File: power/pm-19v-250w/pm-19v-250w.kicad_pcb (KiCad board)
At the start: 4 copper layers, 58.4 x 22.9 mm, 58 parts, among them J1 Brick 1/8 (DOSA), J2 Aux, Q1 BSC070N10NS5, Q2 BSC070N10NS5, Q3 BSC070N10NS5, Q4 BSC070N10NS5, U1 LTC7810, U2 MCP65R46-1.21, U3 MCP65R46-1.21

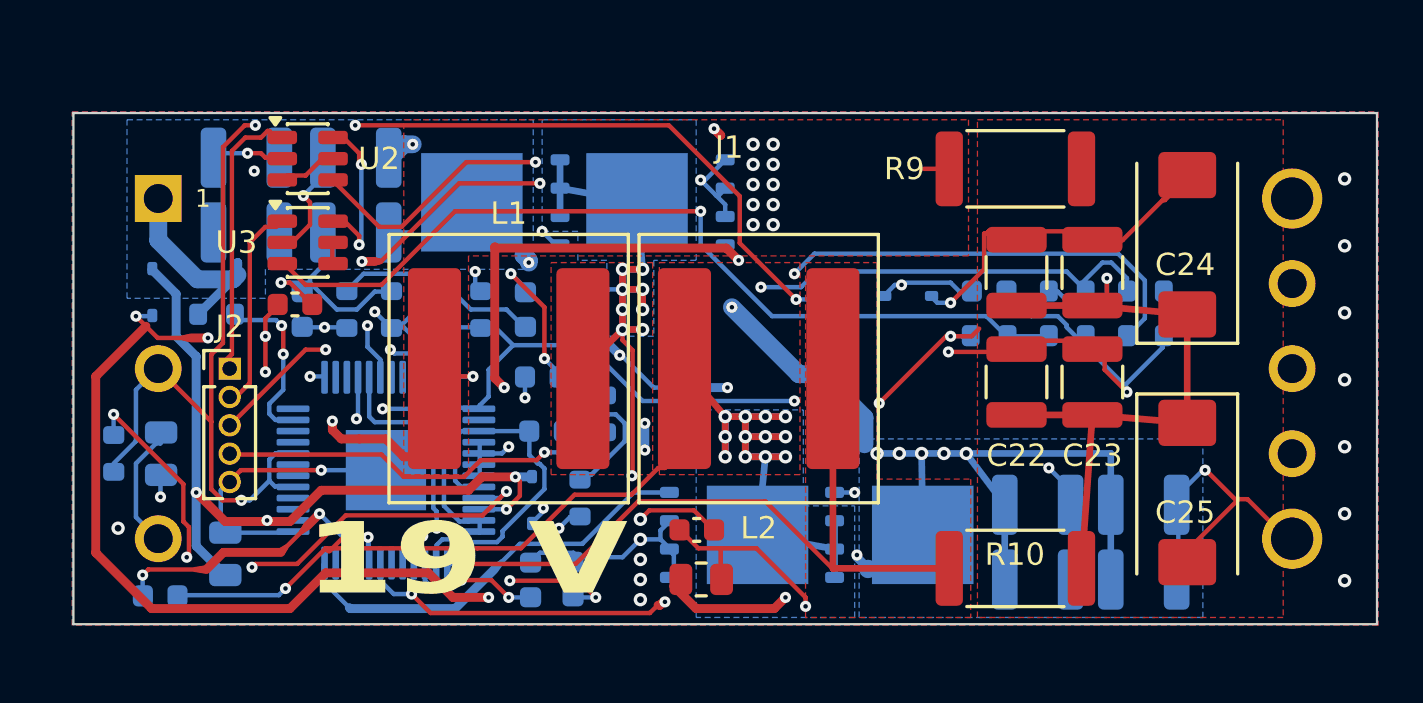
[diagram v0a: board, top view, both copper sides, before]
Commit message: pm-19v-250w: new placement (XAL1510 on F, polymers C24/C25 and phase FETs on B, screw keep-outs clear, aux pads on B at the output end); screw via ring pads 0.65 mm (annular); board rebuilt from the netlist, unrouted
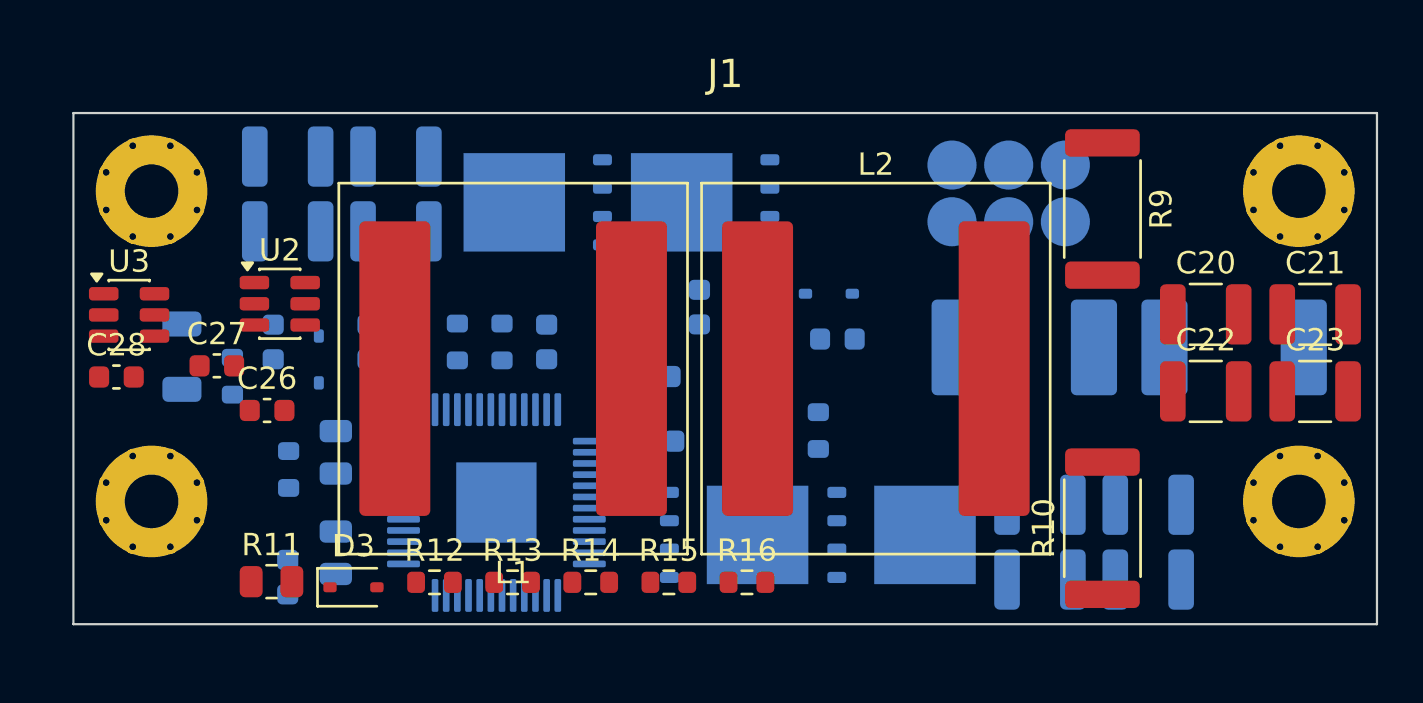
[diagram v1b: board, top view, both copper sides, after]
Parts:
- removed TH1: 10k NTC, Resistor_SMD:R_0603_1608Metric
- C24, C25: value 100u -> 100u 35V polymer 7360-20; footprint Capacitor_Tantalum_SMD:CP_EIA-7343-31_Kemet-D -> Capacitor_Tantalum_SMD:CP_EIA-7360-38_Kemet-E; moved to B.Cu
- C26, D3, R12, R13, R14, R15: moved to F.Cu
- J1: value Brick 1/8 (DOSA) -> Screw pads S1-S4; footprint pm:Brick_Eighth_DOSA -> pm:PM_Mount_M2
- J2: value Aux -> Aux pads 2x3; footprint Connector_PinHeader_1.27mm:PinHeader_1x05_P1.27mm_Vertical -> pm:PM_Aux_Pads_2x03
- L1, L2: value 22u Isat>=12A -> 22u XAL1510-223; footprint Inductor_SMD:L_Coilcraft_XAL1010-XXX -> Inductor_SMD:L_Coilcraft_XAL1510-223
- R10, R9: value 8m 2512 -> 7m 2512
- R16: value 10k (ID) -> 22k (ID); moved to F.Cu
- R4: value 12.4k -> 13.7k
- R5: value 19.6k -> 18.2k
- R8: value 15k -> 13k
- moved J2 35.8 mm to (141.9, 103.6)
- moved C26 32.8 mm to (108.7, 113.3)
- moved R12 31.2 mm to (116.2, 121.0)
- moved R13 31.2 mm to (119.7, 121.0)
- moved R3 29.3 mm to (104.9, 110.9)
- moved C19 29.2 mm to (130.7, 110.1)
- moved D3 28.1 mm to (112.5, 121.2)
- moved C28 26.9 mm to (101.9, 111.8)
- moved R14 21.0 mm to (123.2, 121.0)
- moved R15 21.0 mm to (126.7, 121.0)
- moved R16 21.0 mm to (130.2, 121.0)
- moved R11 19.3 mm to (108.9, 121.0)
- moved D2 16.2 mm to (133.8, 108.1), turned to 0 degrees
- moved C17 16.0 mm to (134.2, 110.1), turned to 0 degrees
- moved C18 13.4 mm to (109.0, 110.3)
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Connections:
- J1 pad 2: /RUN -> GND
- J1 pad 4: GND -> /VOUT
- J2 pad 4: /TEMP -> /RUN
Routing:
- net GND: track 185.9 -> 0.00 mm, vias 36 -> 0
- net /VIN: track 80.7 -> 0.00 mm, vias 11 -> 0
- net /VAUX: track 78.0 -> 0.00 mm, vias 6 -> 0
- net /BOOST1: track 75.8 -> 0.00 mm, vias 8 -> 0
- net /VOUT: track 73.3 -> 0.00 mm, vias 4 -> 0
- net /RUN: track 62.5 -> 0.00 mm, vias 4 -> 0
- net /SW2: track 61.0 -> 0.00 mm, vias 14 -> 0
- net /SW1: track 53.0 -> 0.00 mm, vias 10 -> 0
- net /ID: track 49.7 -> 0.00 mm, vias 2 -> 0
- net Net-(U2--): track 42.3 -> 0.00 mm, vias 2 -> 0
- net Net-(U3-+): track 39.3 -> 0.00 mm, vias 1 -> 0
- net /DRVCC: track 35.7 -> 0.00 mm, vias 4 -> 0
- net /SNS1P: track 35.6 -> 0.00 mm, vias 3 -> 0
- net /SNS2P: track 33.9 -> 0.00 mm, vias 1 -> 0
- net /OVLO: track 30.9 -> 0.00 mm, vias 5 -> 0
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- removed copper zone on F.Cu, net /SNS1P
- removed copper zone on F.Cu, net /SNS2P
- removed copper zone on B.Cu, net /SW1
- removed copper zone on F.Cu, net /SW1
- removed copper zone on B.Cu, net /SW2
- removed copper zone on F.Cu, net /SW2
- removed copper zone on B.Cu, net /VIN
- removed copper zone on F.Cu, net /VOUT
- removed copper zone on B.Cu, net GND
- removed copper zone on F.Cu, net GND
- removed copper zone on In2.Cu, net GND
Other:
- board text removed: "19 V"

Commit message: pm-19v-250w: placement reworked for the via fields (U1 left/up for the phase 2 fan-out, D2/C19 beside SW2, RUN divider on F at the input end), power.py: B/F pours, In1 VIN feed, GND islands under the input caps, via fields; backbone pad side by pad layer
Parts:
- R15, R16, U3: moved to B.Cu
- R3, R4: moved to F.Cu
- moved U3 46.9 mm to (148.8, 102.0)
- moved C15 24.6 mm to (103.5, 109.6)
- moved C13 20.7 mm to (105.3, 110.4), turned to 90 degrees
- moved R16 20.6 mm to (135.2, 101.1)
- moved R15 20.3 mm to (109.8, 109.7)
- moved C17 19.3 mm to (115.0, 109.7)
- moved C14 18.3 mm to (131.4, 108.8)
- moved R8 15.6 mm to (130.6, 112.7)
- moved C26 13.4 mm to (119.7, 121.0)
- moved R7 11.8 mm to (128.7, 112.6)
- moved R13 11.5 mm to (131.2, 121.0)
- moved R14 11.5 mm to (134.7, 121.0)
- moved R12 11.5 mm to (127.7, 121.0)
- moved C28 11.2 mm to (108.7, 120.8)
- moved R6 10.4 mm to (129.4, 108.8)
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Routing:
- net /VIN: track 0.00 -> 69.9 mm, vias 0 -> 9
- net GND: track 0.00 -> 68.1 mm, vias 0 -> 38
- net /VOUT: track 0.00 -> 46.8 mm, vias 0 -> 5
- net /SNS1P: track 0.00 -> 42.8 mm
- net /SW1: track 0.00 -> 32.5 mm, vias 0 -> 12
- net /SW2: track 0.00 -> 25.6 mm, vias 0 -> 8
- added copper zone on F.Cu, net /SNS1P
- added copper zone on F.Cu, net /SNS2P
- added copper zone on B.Cu, net /SW1
- added copper zone on F.Cu, net /SW1
- added copper zone on B.Cu, net /SW2
- added copper zone on F.Cu, net /SW2
- added copper zone on B.Cu, net /VIN
- added copper zone on In1.Cu, net /VIN
- added copper zone on B.Cu, net /VOUT
- added copper zone on F.Cu, net /VOUT
- added copper zone on B.Cu, net GND
- added copper zone on F.Cu, net GND

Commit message: pm-19v-250w: KRT first pass, 25/32 nets routed, 10 opens in the U1 gate-drive fan-out (TG1 TG2 BOOST1 BOOST2 DRVCC INTVCC OVLO); 0 copper clearance errors, parity clean; handoff updated
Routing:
- net GND: track 68.1 -> 199.9 mm, vias 38 -> 46
- net /VAUX: track 0.00 -> 90.0 mm, vias 0 -> 12
- net /RUN: track 0.00 -> 60.6 mm, vias 0 -> 4
- net Net-(U3-+): track 0.00 -> 60.6 mm, vias 0 -> 5
- net /VOUT: track 46.8 -> 106.2 mm, vias 5 -> 8
- net /OVLO: track 0.00 -> 50.2 mm, vias 0 -> 4
- net /OV_KILL: track 0.00 -> 38.8 mm, vias 0 -> 1
- net /VIN: track 69.9 -> 105.9 mm, vias 9 -> 13
- net Net-(U2--): track 0.00 -> 34.5 mm, vias 0 -> 2
- net Net-(C13-Pad1): track 0.00 -> 33.1 mm, vias 0 -> 4
- net Net-(U1-VFB1): track 0.00 -> 30.4 mm, vias 0 -> 4
- net /SNS2P: track 0.00 -> 30.2 mm, vias 0 -> 1
- net /SW2: track 25.6 -> 54.0 mm, vias 8 -> 10
- net Net-(U1-ITH1): track 0.00 -> 27.8 mm, vias 0 -> 2
- net /SW1: track 32.5 -> 58.2 mm, vias 12 -> 15
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- added copper zone on In2.Cu, net GND

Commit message: pm-19v-250w: U1 neighbourhood reorganised for hand-routing the gate drive: U1 small-signal passives to 0402 (C10 C12-C19 R5-R8, JLC parts), VFB/ITH1 network in a pocket above pins 45-47, corridor above the phase 1 drive pins and a TG1 lane kept free, bootstraps C18/C19 beside their switch nodes; VIN band under C1-C4 narrowed to 108.2; packer step 0.05, gap 0.2; unrouted
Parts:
- C10, C12, C13, C14, C15, C16, C17, C18, C19: footprint Capacitor_SMD:C_0603_1608Metric -> Capacitor_SMD:C_0402_1005Metric
- R15, U3: moved to F.Cu
- R5, R6, R7, R8: footprint Resistor_SMD:R_0603_1608Metric -> Resistor_SMD:R_0402_1005Metric
- moved U3 42.8 mm to (106.9, 110.4)
- moved C28 41.2 mm to (149.8, 121.8)
- moved D1 30.5 mm to (132.6, 108.1)
- moved R15 29.8 mm to (137.4, 120.9)
- moved C18 27.0 mm to (128.4, 111.9)
- moved C15 25.6 mm to (129.0, 108.1)
- moved C13 14.7 mm to (120.0, 110.1), turned to 0 degrees
- moved R3 14.1 mm to (109.4, 121.3), turned to 0 degrees
- moved R8 13.1 mm to (117.8, 110.1), turned to 0 degrees
- moved R6 10.9 mm to (118.5, 108.9), turned to 0 degrees
- moved C14 10.9 mm to (120.7, 107.6), turned to 0 degrees
- moved R7 8.86 mm to (120.7, 108.9), turned to 0 degrees
- moved C16 8.70 mm to (109.9, 113.0), turned to 90 degrees
- moved C10 8.50 mm to (128.4, 114.0), turned to 90 degrees
- moved C17 7.39 mm to (109.9, 115.1), turned to 90 degrees
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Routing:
- net GND: track 199.9 -> 67.3 mm, vias 46 -> 37
- net /VAUX: track 90.0 -> 0.00 mm, vias 12 -> 0
- net /RUN: track 60.6 -> 0.00 mm, vias 4 -> 0
- net Net-(U3-+): track 60.6 -> 0.00 mm, vias 5 -> 0
- net /VOUT: track 106.2 -> 46.8 mm, vias 8 -> 5
- net /OVLO: track 50.2 -> 0.00 mm, vias 4 -> 0
- net /OV_KILL: track 38.8 -> 0.00 mm, vias 1 -> 0
- net /VIN: track 105.9 -> 69.9 mm, vias 13 -> 9
- net Net-(U2--): track 34.5 -> 0.00 mm, vias 2 -> 0
- net Net-(C13-Pad1): track 33.1 -> 0.00 mm, vias 4 -> 0
- net Net-(U1-VFB1): track 30.4 -> 0.00 mm, vias 4 -> 0
- net /SNS2P: track 30.2 -> 0.00 mm, vias 1 -> 0
- net /SW2: track 54.0 -> 25.6 mm, vias 10 -> 8
- net Net-(U1-ITH1): track 27.8 -> 0.00 mm, vias 2 -> 0
- net /SW1: track 58.2 -> 32.5 mm, vias 15 -> 12
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- removed copper zone on In2.Cu, net GND

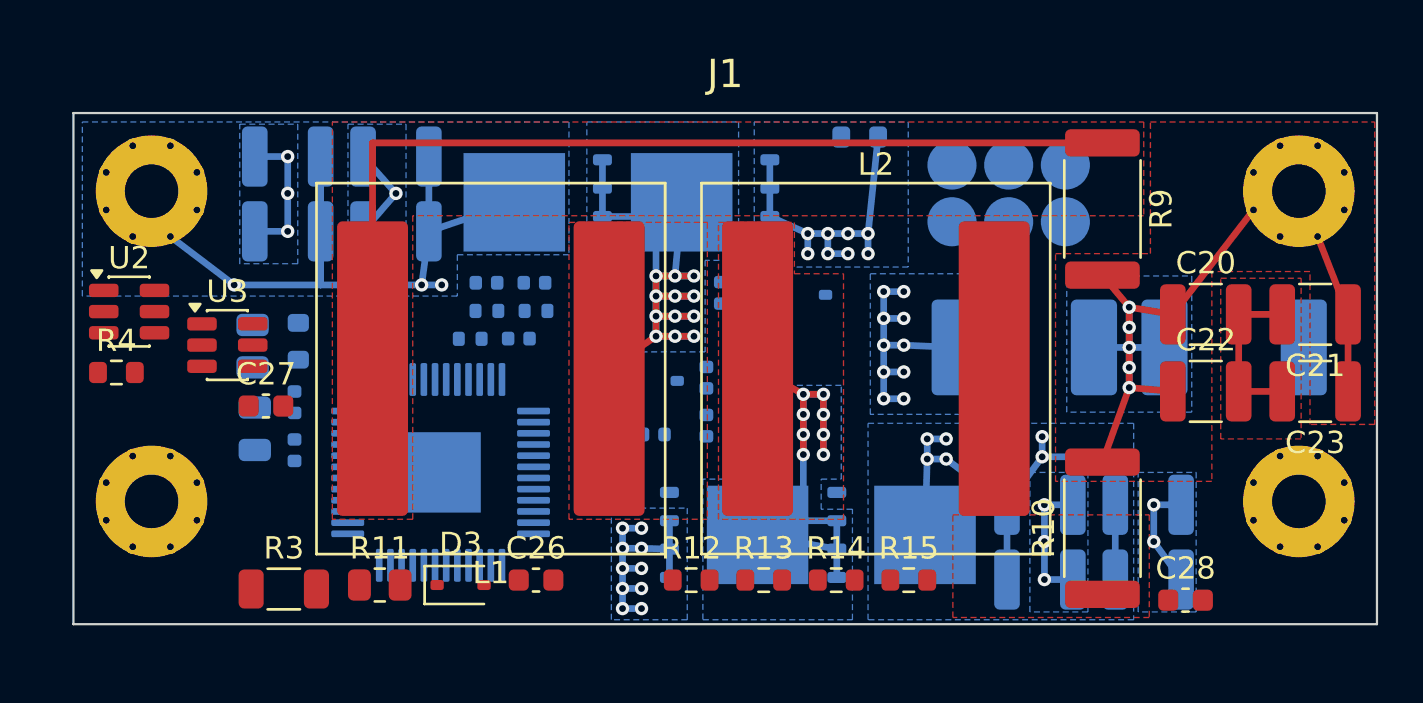
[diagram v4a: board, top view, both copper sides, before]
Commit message: pm-19v-250w: KRT pass on the reorganised placement: 22/32 routed, 14 opens all at U1 pins (TG1 TG2 BOOST1 BOOST2 DRVCC INTVCC RUN OVLO VIN_IC VFB), left for hand routing; 0 copper clearance errors, parity clean
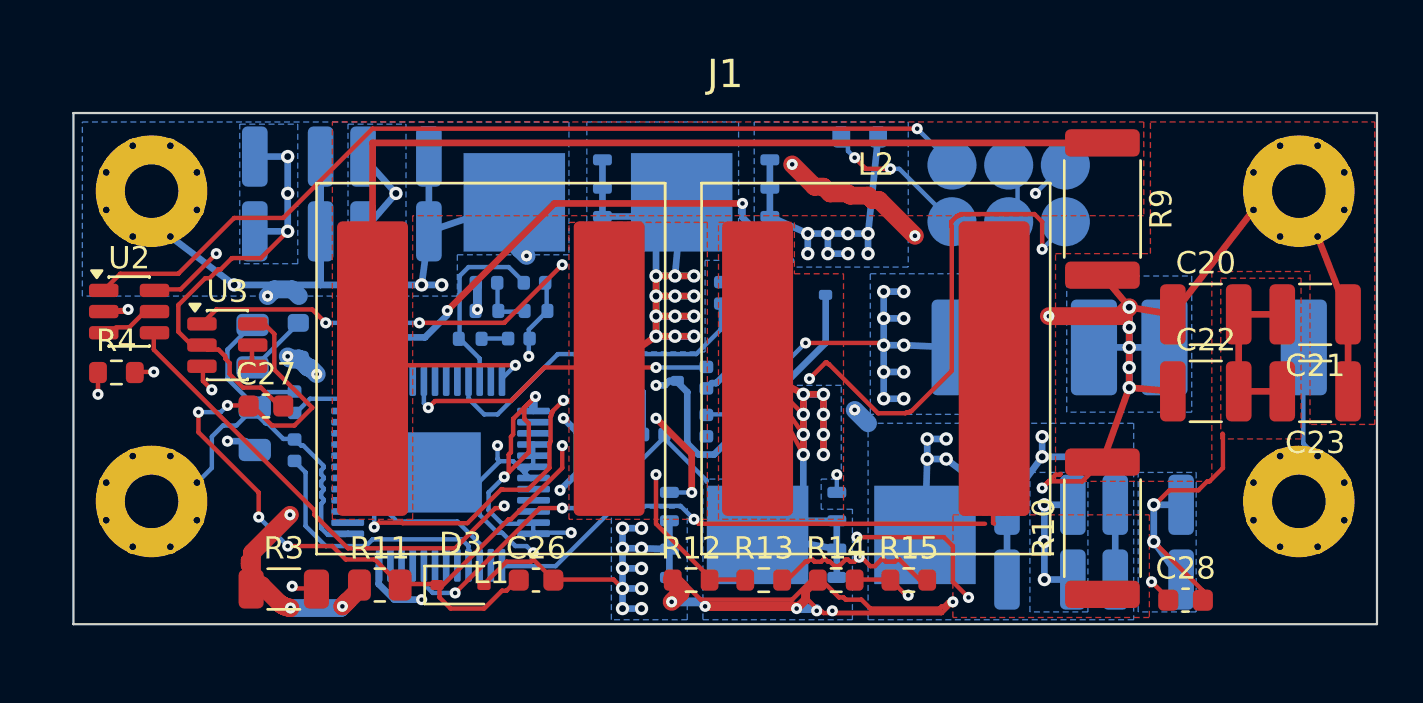
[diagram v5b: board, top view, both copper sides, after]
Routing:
- net /VOUT: track 46.8 -> 183.4 mm, vias 5 -> 19
- net GND: track 67.3 -> 173.7 mm, vias 37 -> 43
- net /VAUX: track 0.00 -> 80.8 mm, vias 0 -> 9
- net /VIN: track 69.9 -> 148.2 mm, vias 9 -> 17
- net /RUN: track 0.00 -> 58.3 mm, vias 0 -> 6
- net Net-(U3-+): track 0.00 -> 43.3 mm, vias 0 -> 2
- net /PGOOD: track 0.00 -> 42.0 mm, vias 0 -> 4
- net /OV_KILL: track 0.00 -> 41.6 mm, vias 0 -> 1
- net /DRVCC: track 0.00 -> 38.2 mm, vias 0 -> 2
- net Net-(U2--): track 0.00 -> 35.5 mm, vias 0 -> 2
- net /SNS2P: track 0.00 -> 30.2 mm, vias 0 -> 1
- net /SW2: track 25.6 -> 54.0 mm, vias 8 -> 10
- net /BG2: track 0.00 -> 23.9 mm, vias 0 -> 5
- net /BG1: track 0.00 -> 21.6 mm, vias 0 -> 2
- net Net-(U1-TRACK/SS1): track 0.00 -> 15.3 mm
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- added copper zone on In2.Cu, net GND

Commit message: pm-19v-250w: U1 turned to rot 0 and moved 2 mm left, phase pairs swapped in placement (Q3/Q4/L2/R10 top = phase 2, Q1/Q2/L1/R9 bottom = phase 1) so each drive group faces its FETs; bootstraps at their pins; gate drive hand-routed (tools/route_drive.py: TG2/SW2/BOOST2 on B, BG2/TG1/BG1 via In1, SW1 on an F lane), DRC clean in the region; rest unrouted
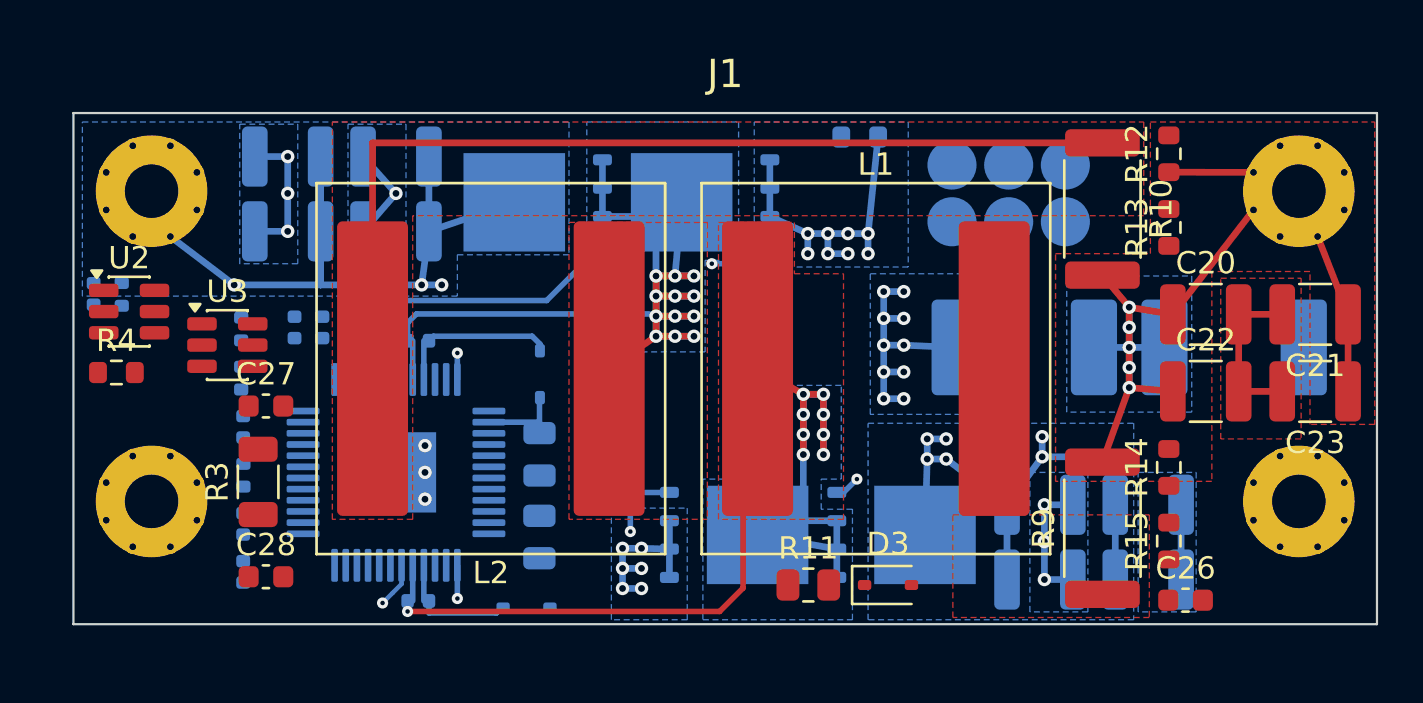
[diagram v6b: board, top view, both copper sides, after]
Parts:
- moved C28 41.2 mm to (108.6, 120.8)
- moved C26 29.1 mm to (149.8, 121.8)
- moved R12 28.7 mm to (149.1, 101.8), turned to 90 degrees
- moved R5 28.1 mm to (102.2, 108.1)
- moved C15 28.1 mm to (100.9, 108.1)
- moved R13 24.1 mm to (149.1, 105.1), turned to 90 degrees
- moved Q1 22.1 mm to (137.1, 118.9), turned to 0 degrees
- moved Q3 22.1 mm to (120.8, 104.0), turned to 180 degrees
- moved R11 19.2 mm to (132.9, 121.1)
- moved D3 19.2 mm to (136.5, 121.1)
- moved D1 18.7 mm to (120.3, 122.2)
- moved C14 18.4 mm to (107.6, 120.6), turned to 90 degrees
- moved L1 17.2 mm to (135.9, 111.5), turned to 0 degrees
- moved L2 17.2 mm to (118.7, 111.5), turned to 180 degrees
- moved C10 16.5 mm to (112.4, 109.6)
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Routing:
- net /VOUT: track 183.4 -> 50.6 mm, vias 19 -> 5
- net GND: track 173.7 -> 62.1 mm, vias 43 -> 34
- net /VAUX: track 80.8 -> 0.00 mm, vias 9 -> 0
- net /VIN: track 148.2 -> 69.9 mm, vias 17 -> 9
- net /RUN: track 58.3 -> 0.00 mm, vias 6 -> 0
- net /SNS1P: track 48.9 -> 0.00 mm, vias 1 -> 0
- net Net-(U3-+): track 43.3 -> 0.00 mm, vias 2 -> 0
- net /PGOOD: track 42.0 -> 0.00 mm, vias 4 -> 0
- net /OV_KILL: track 41.6 -> 0.00 mm, vias 1 -> 0
- net Net-(U2--): track 35.5 -> 0.00 mm, vias 2 -> 0
- net /DRVCC: track 38.2 -> 3.37 mm, vias 2 -> 0
- net /TG1: track 0.00 -> 28.0 mm, vias 0 -> 2
- net Net-(U1-TRACK/SS1): track 15.3 -> 0.00 mm
- net Net-(U1-ITH2): track 14.5 -> 0.00 mm
- net /TG2: track 0.80 -> 13.9 mm, vias 1 -> 0
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- removed copper zone on In2.Cu, net GND
